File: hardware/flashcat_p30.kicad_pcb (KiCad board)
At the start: 4 copper layers, 51 x 37 mm, 15 parts, among them J1 EC56 J1 (control/data), J2 EC56 J2 (address), U1 PC28F256P30T85, U2 TLV75518PDBV

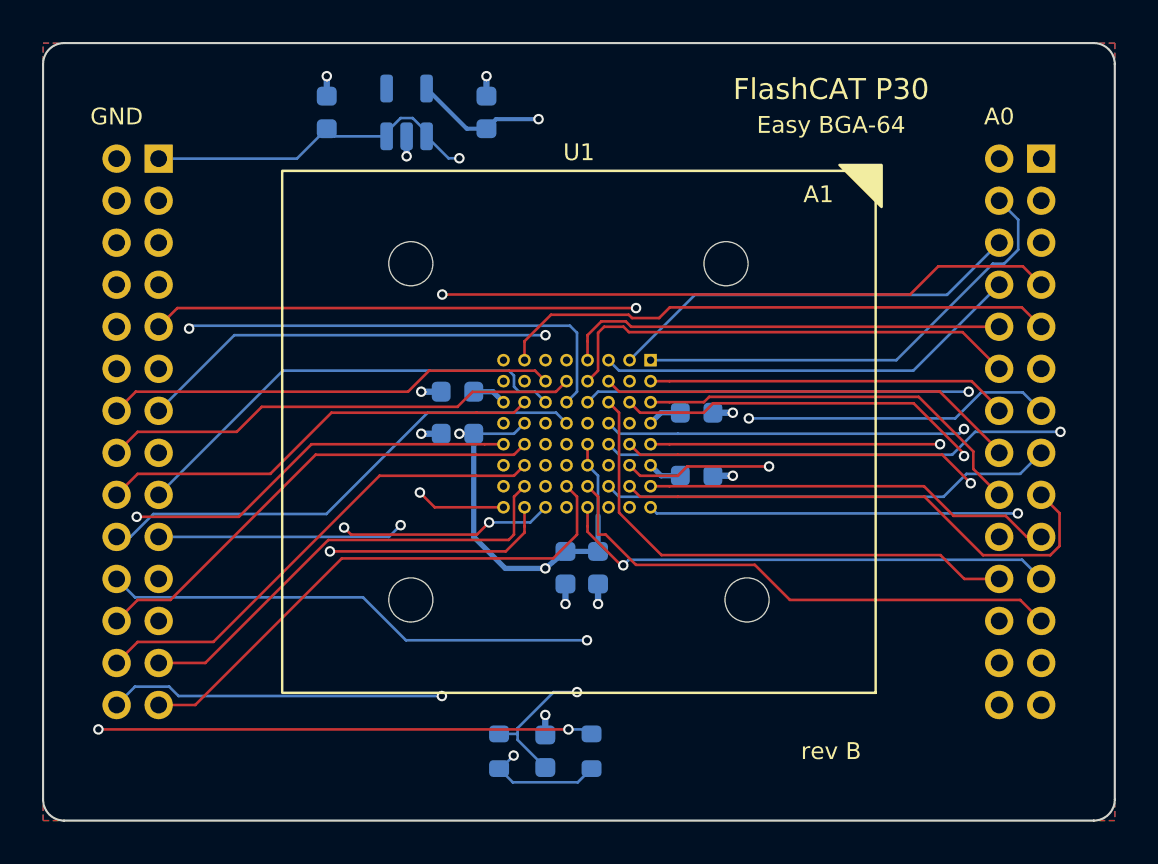
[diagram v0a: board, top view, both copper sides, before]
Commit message: feat(hardware): wire balls B8/H1 to header A26/A27 for Micron P30-65nm 1/2 Gbit parts
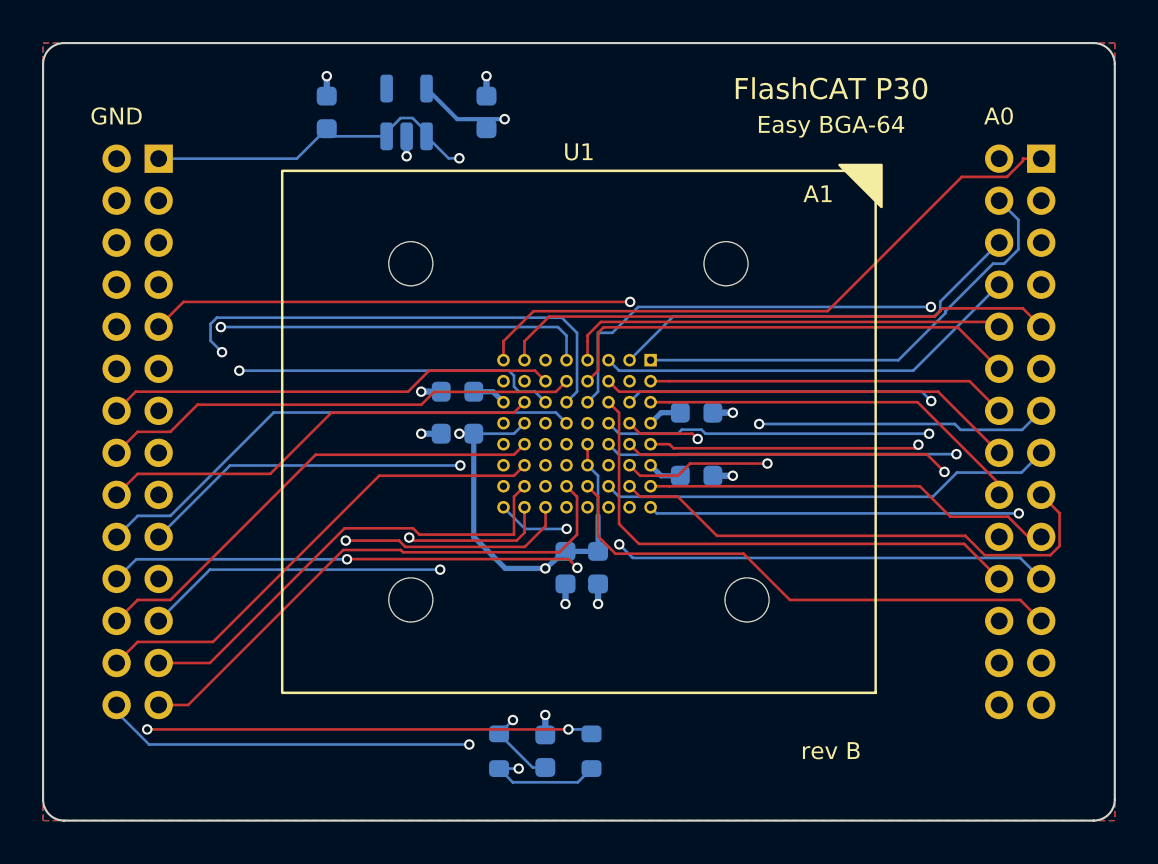
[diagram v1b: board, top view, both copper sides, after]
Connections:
- J2 pad 1: unconnected-(J2-A27/RB1-Pad1) -> /A27
- J2 pad 3: unconnected-(J2-A26/RB2-Pad3) -> /A26
- U1 pad B8: unconnected-(U1-RFU-PadB8) -> /A26
- U1 pad H1: unconnected-(U1-RFU-PadH1) -> /A27
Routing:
- net /A27: track 0.00 -> 30.2 mm
- net /A26: track 0.00 -> 25.6 mm
- net /A24: track 43.6 -> 34.8 mm, vias 2 -> 1
- net /A11: track 30.7 -> 36.7 mm
- net /DQ4: track 34.1 -> 28.6 mm, vias 1 -> 2
- net /~{CE}: track 28.9 -> 34.3 mm, vias 1 -> 2
- net /A15: track 33.5 -> 28.7 mm
- net /DQ7: track 27.2 -> 30.7 mm
- net /DQ13: track 24.3 -> 21.6 mm
- net +1V8: track 39.7 -> 37.2 mm
- net /WAIT: track 53.1 -> 51.0 mm
- net /~{WE}: track 26.9 -> 28.7 mm
- net /A12: track 29.6 -> 27.9 mm
- net /DQ8: track 21.5 -> 23.0 mm
- net /~{OE}: track 27.5 -> 28.8 mm, vias 2 -> 1
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
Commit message: feat(hardware): switch to the HMILU BGA64-1.0-TP21NS 10x13 mm socket on a 51x33 mm board
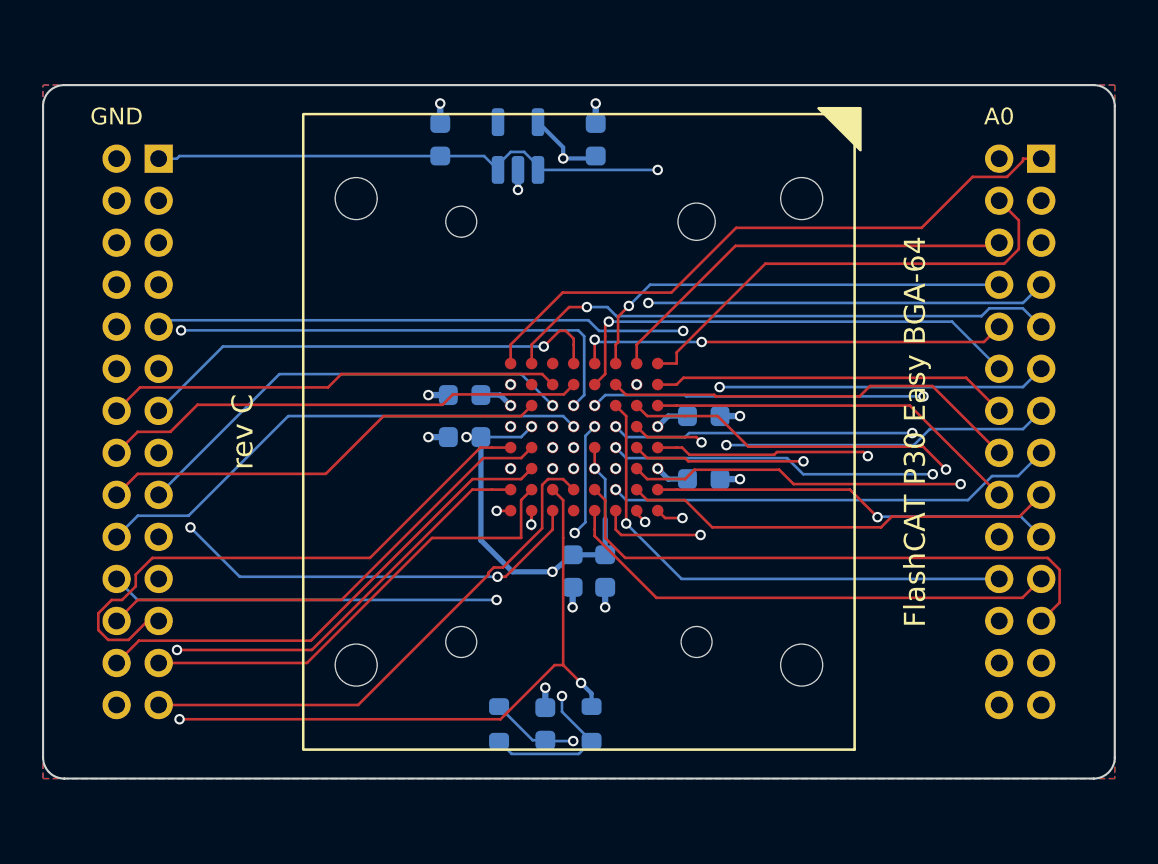
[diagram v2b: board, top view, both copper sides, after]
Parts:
- U1: footprint flashcat_p30:Sensata_CBG064-087G -> flashcat_p30:HMILU_BGA64-1.0-TP21NS
- moved C1 5.55 mm to (141.9, 91.1)
- moved U2 5.54 mm to (145.6, 91.4)
- moved C2 5.36 mm to (149.3, 91.1)
- moved C9 1.30 mm to (146.9, 118.9)
- moved R1 1.30 mm to (144.7, 118.9)
- moved R2 1.30 mm to (149.1, 118.9)
- moved C3 0.38 mm to (154.4, 104.2)
- moved C5 0.38 mm to (154.4, 107.2)
- moved C6 0.38 mm to (143.1, 103.2)
- moved C7 0.38 mm to (149.8, 111.6)
- moved C8 0.38 mm to (143.1, 105.2)
- moved C4 0.38 mm to (148.2, 111.6)
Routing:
- net /A11: track 36.7 -> 28.1 mm, vias 1 -> 2
- net /~{WE}: track 28.7 -> 36.6 mm
- net /DQ7: track 30.7 -> 23.9 mm
- net /DQ13: track 21.6 -> 27.4 mm, vias 1 -> 0
- net /~{OE}: track 28.8 -> 34.2 mm, vias 1 -> 2
- net /A25: track 24.8 -> 29.5 mm
- net +1V8: track 37.2 -> 41.7 mm, vias 1 -> 3
- net /A19: track 24.8 -> 20.6 mm
- net /A21: track 23.1 -> 25.5 mm, vias 1 -> 2
- net /A9: track 22.6 -> 20.2 mm
- net /A26: track 25.6 -> 27.9 mm, vias 0 -> 1
- net /A16: track 25.3 -> 27.6 mm
- net /A13: track 26.9 -> 24.7 mm
- net VCC_PROG: track 71.8 -> 73.8 mm, vias 4 -> 8
- net /A14: track 28.8 -> 27.1 mm
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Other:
- board size 51 x 37 mm -> 51 x 33 mm
- board text added: "EC 56-pin header rev C 2026-10"
- board text added: "FlashCAT P30 Easy BGA-64"
- board text added: "HMILU BGA64-1.0-TP21NS socket"
- board text added: "rev C"
- board text removed: "Easy BGA-64"
- board text removed: "FlashCAT P30"
- board text removed: "Sensata CBG064-087G + EC 56-pin header"
- board text removed: "rev B"
- board text removed: "rev B 2026-09"

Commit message: fix(hardware): size socket locator drills for fab hole tolerance and raise silkscreen to 1.0 mm
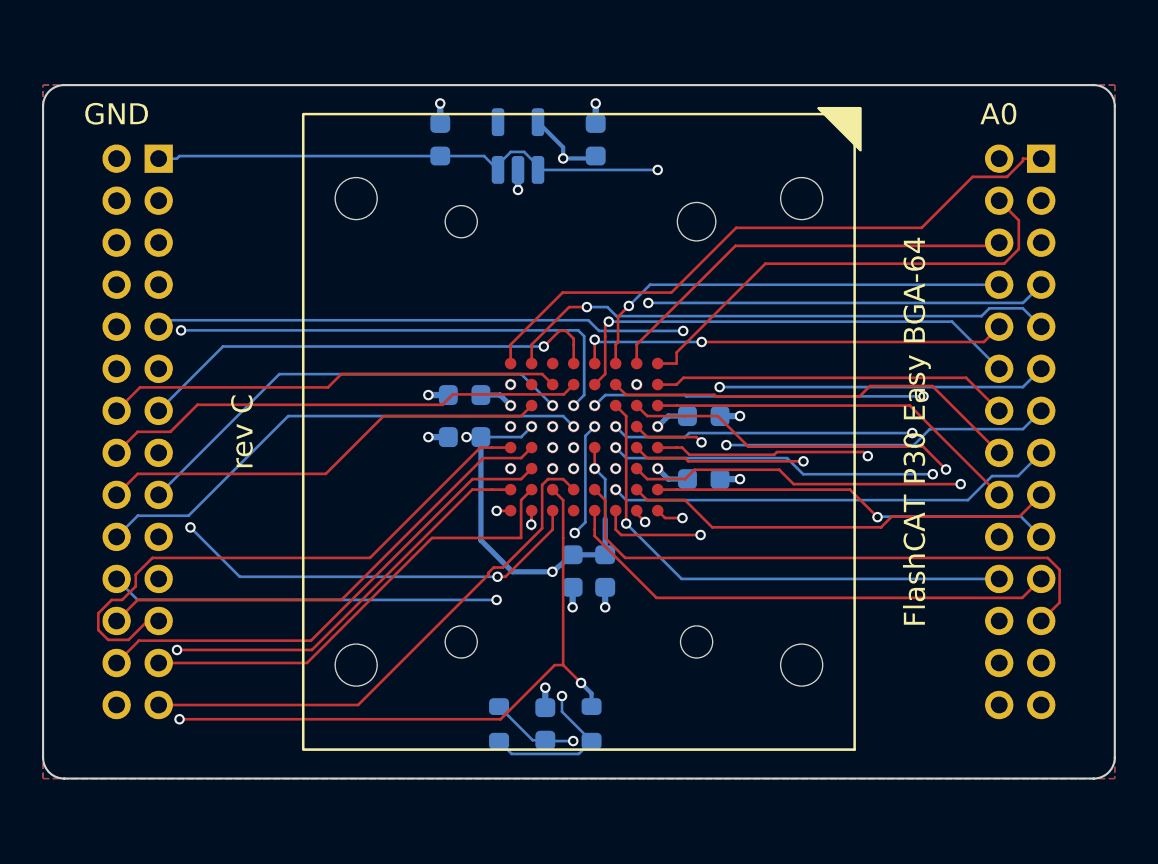
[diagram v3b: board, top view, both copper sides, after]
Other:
- board text added: "HMILU BGA64-1.0-TP21NS"
- board text added: "rev C 2026-10"
- board text removed: "EC 56-pin header rev C 2026-10"
- board text removed: "FlashCAT P30 Easy BGA-64 adapter"
- board text removed: "HMILU BGA64-1.0-TP21NS socket"
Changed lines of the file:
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@@
 			(effects
 				(font
-					(size 0.8 0.8)
-					(thickness 0.12)
+					(size 1 1)
+					(thickness 0.15)
 				)
 			)
@@
 		(pad "" np_thru_hole circle
 			(at -5.6 -10 180)
-			(size 1.475 1.475)
-			(drill 1.475)
+			(size 1.53 1.53)
+			(drill 1.53)
 			(layers "*.Cu" "*.Mask")
 		)
 		(pad "" np_thru_hole circle
 			(at -5.6 10 180)
-			(size 1.775 1.775)
-			(drill 1.775)
+			(size 1.83 1.83)
+			(drill 1.83)
 			(layers "*.Cu" "*.Mask")
 		)
 		(pad "" np_thru_hole circle
 			(at 5.6 -10 180)
-			(size 1.475 1.475)
-			(drill 1.475)
+			(size 1.53 1.53)
+			(drill 1.53)
 			(layers "*.Cu" "*.Mask")
 		)
 		(pad "" np_thru_hole circle
 			(at 5.6 10 180)
-			(size 1.475 1.475)
-			(drill 1.475)
+			(size 1.53 1.53)
+			(drill 1.53)
 			(layers "*.Cu" "*.Mask")
 		)
@@
 			(effects
 				(font
-					(size 0.8 0.8)
-					(thickness 0.12)
+					(size 1 1)
+					(thickness 0.15)
 				)
 				(justify mirror)
@@
 		(tags "capacitor")
 		(property "Reference" "C8"
-			(at 0 -1.2 0)
+			(at -0.000001 -1.2 0)
 			(layer "B.SilkS")
 			(effects
 				(font
-					(size 0.8 0.8)
-					(thickness 0.12)
+					(size 1 1)
+					(thickness 0.15)
 				)
 				(justify mirror)
@@
 		(tags "capacitor")
 		(property "Reference" "C6"
-			(at 0 1.2 0)
+			(at -0.000001 1.2 0)
 			(layer "B.SilkS")
 			(effects
 				(font
-					(size 0.8 0.8)
-					(thickness 0.12)
+					(size 1 1)
+					(thickness 0.15)
 				)
 				(justify mirror)
@@
 			(effects
 				(font
-					(size 0.8 0.8)
-					(thickness 0.12)
+					(size 1 1)
+					(thickness 0.15)
 				)
 				(justify mirror)
@@
 		(tags "SOT TO_SOT_SMD")
 		(property "Reference" "U2"
-			(at 2.2 0 0)
+			(at 0 -2.299999 90)
 			(layer "B.SilkS")
 			(effects
 				(font
-					(size 0.8 0.8)
-					(thickness 0.12)
+					(size 1 1)
+					(thickness 0.15)
 				)
 				(justify mirror)
@@
 			(effects
 				(font
-					(size 0.8 0.8)
-					(thickness 0.12)
+					(size 1 1)
+					(thickness 0.15)
 				)
 				(justify mirror)
@@
 			(effects
 				(font
-					(size 0.8 0.8)
-					(thickness 0.12)
+					(size 1 1)
+					(thickness 0.15)
 				)
 				(justify mirror)
@@
 			(effects
 				(font
-					(size 0.8 0.8)
-					(thickness 0.12)
+					(size 1 1)
+					(thickness 0.15)
 				)
 				(justify mirror)
@@
 		(tags "capacitor")
 		(property "Reference" "C5"
-			(at 0 1.2 0)
+			(at -0.000001 1.2 0)
 			(layer "B.SilkS")
 			(effects
 				(font
-					(size 0.8 0.8)
-					(thickness 0.12)
+					(size 1 1)
+					(thickness 0.15)
 				)
 				(justify mirror)
@@
 			(effects
 				(font
-					(size 0.8 0.8)
-					(thickness 0.12)
+					(size 1 1)
+					(thickness 0.15)
 				)
 				(justify mirror)
@@
 			(effects
 				(font
-					(size 0.8 0.8)
-					(thickness 0.12)
+					(size 1 1)
+					(thickness 0.15)
 				)
 				(justify mirror)
@@
 		(tags "capacitor")
 		(property "Reference" "C3"
-			(at 0 -1.2 0)
+			(at -0.000001 -1.2 0)
 			(layer "B.SilkS")
 			(effects
 				(font
-					(size 0.8 0.8)
-					(thickness 0.12)
+					(size 1 1)
+					(thickness 0.15)
 				)
 				(justify mirror)
@@
 	)
 	(gr_text "GND"
-		(at 126.5 90 0)
+		(at 126.5 89.9 0)
 		(layer "F.SilkS")
 		(effects
 			(font
-				(size 0.8 0.8)
-				(thickness 0.12)
+				(size 1 1)
+				(thickness 0.15)
 			)
 		)
 	)
 	(gr_text "A0"
-		(at 168.5 90 0)
+		(at 168.5 89.9 0)
 		(layer "F.SilkS")
 		(effects
 			(font
-				(size 0.8 0.8)
-				(thickness 0.12)
+				(size 1 1)
+				(thickness 0.15)
 			)
 		)
@@
 		)
 	)
-	(gr_text "FlashCAT P30 Easy BGA-64 adapter"
-		(at 131.9 105 90)
+	(gr_text "FlashCAT P30 Easy BGA-64"
+		(at 131.7 105 90)
 		(layer "B.SilkS")
 		(effects
 			(font
-				(size 0.8 0.8)
-				(thickness 0.12)
+				(size 1 1)
+				(thickness 0.15)
 			)
 			(justify mirror)
 		)
 	)
-	(gr_text "HMILU BGA64-1.0-TP21NS socket"
+	(gr_text "HMILU BGA64-1.0-TP21NS"
 		(at 133.5 105 90)
 		(layer "B.SilkS")
 		(effects
 			(font
-				(size 0.8 0.8)
-				(thickness 0.12)
+				(size 1 1)
+				(thickness 0.15)
 			)
 			(justify mirror)
 		)
 	)
-	(gr_text "EC 56-pin header  rev C  2026-10"
+	(gr_text "rev C  2026-10"
 		(at 164.5 105 90)
 		(layer "B.SilkS")
 		(effects
 			(font
-				(size 0.8 0.8)
-				(thickness 0.12)
+				(size 1 1)
+				(thickness 0.15)
 			)
 			(justify mirror)
